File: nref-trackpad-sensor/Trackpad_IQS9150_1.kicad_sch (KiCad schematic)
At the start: 49 parts, among them CN1 FPC_6PIN, IC1 IQS9150-000QFR

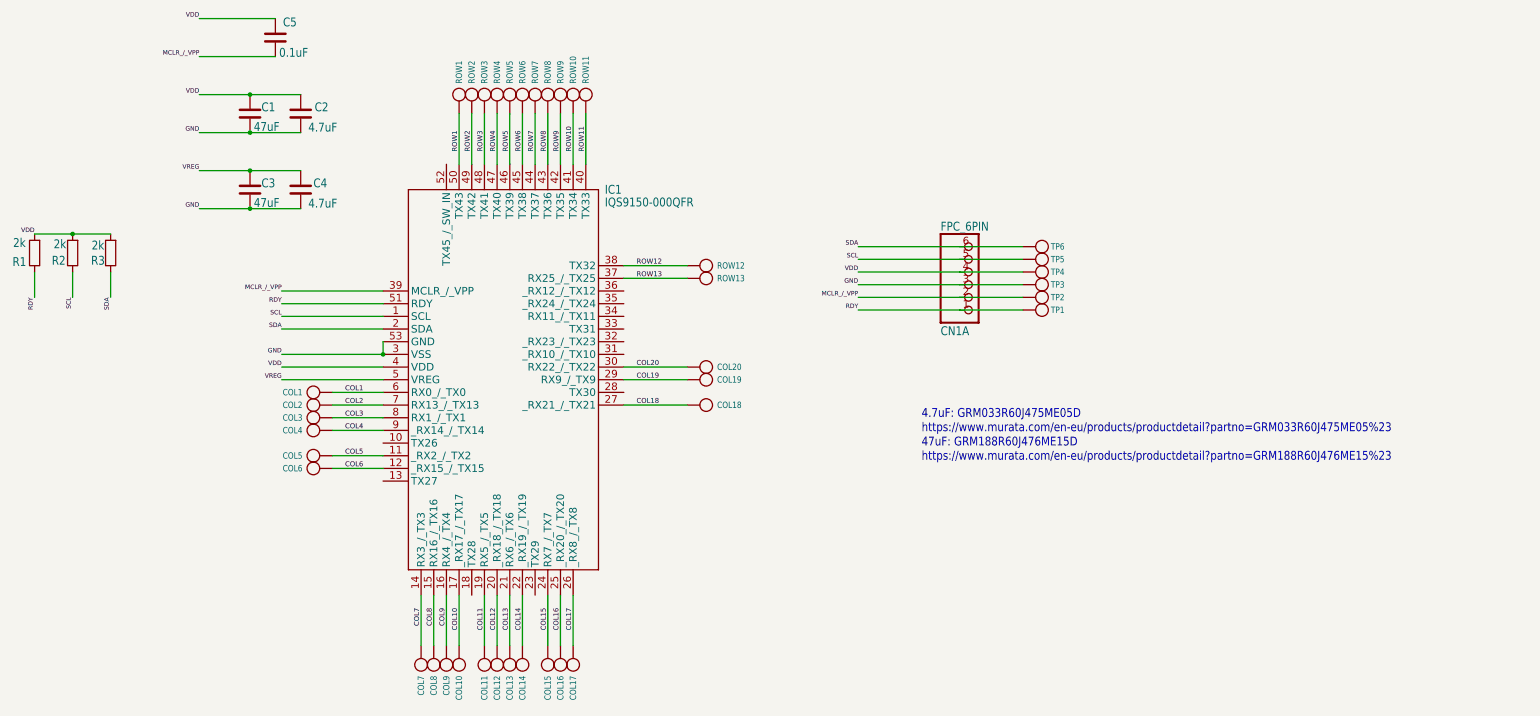
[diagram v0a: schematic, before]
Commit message: trackpad sensor: redesign pcb shape for production
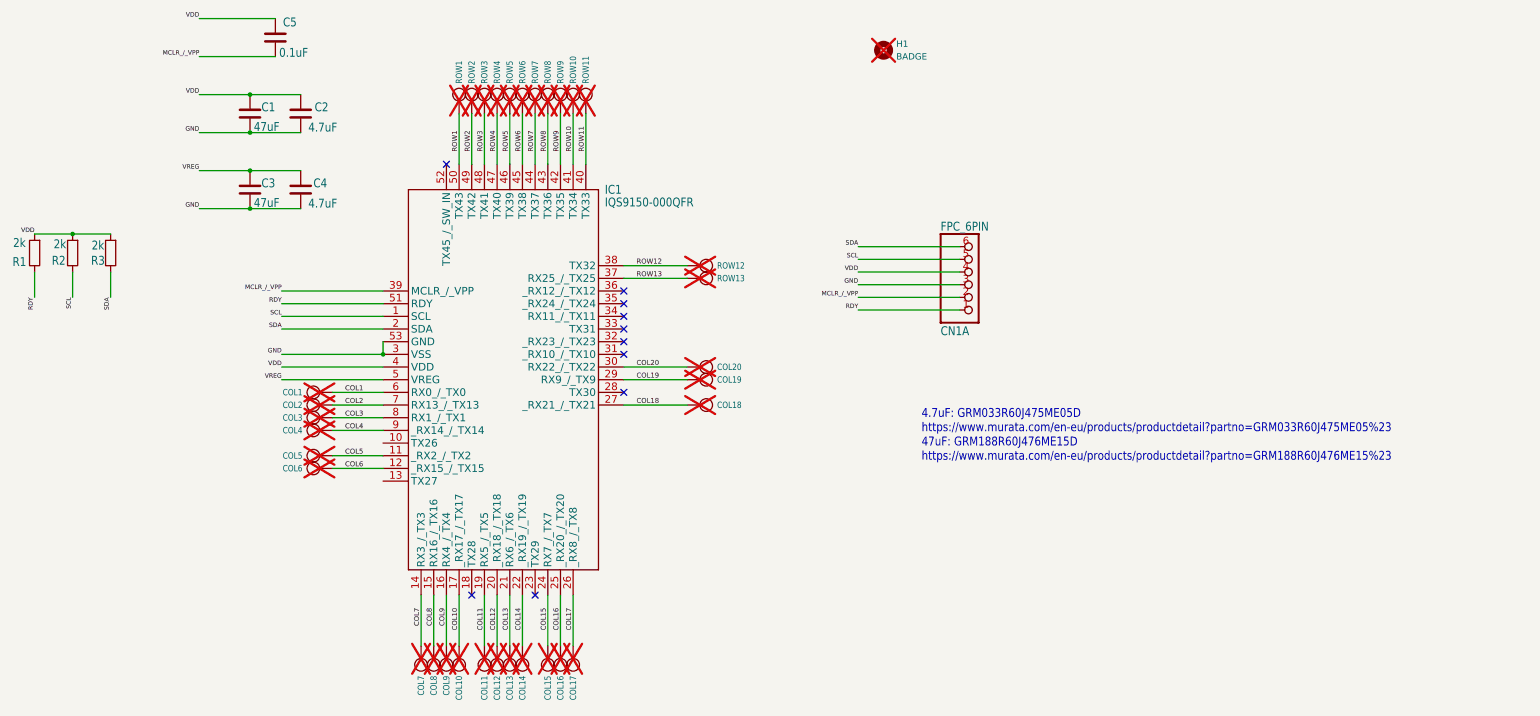
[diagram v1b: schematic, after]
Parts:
- removed TP1, TP2, TP3, TP4, TP5, TP6: TESTPOINTROUND1.5MMNO, Trackpad_IQS9150:TESTPOINT_ROUND_1.5MM_NO, symbol Trackpad_IQS9150:TESTPOINTROUND1.5MMNO
- added H1: BADGE, footprints:nref-tpsensor-badge, symbol Mechanical:MountingHole
- C1, C3: LCSC (none) -> C140782; MPN (none) -> GRM188R60J476ME15D; Manufacturer (none) -> Murata
- C2, C4: footprint Capacitor_SMD:C_0201_0603Metric -> Capacitor_SMD:C_0402_1005Metric; LCSC (none) -> C23733; MPN (none) -> CL05A475MP5NRNC; Manufacturer (none) -> Samsung
- C5: footprint Capacitor_SMD:C_0201_0603Metric -> Capacitor_SMD:C_0402_1005Metric; LCSC (none) -> C1525; MPN (none) -> CL05B104KO5NNNC; Manufacturer (none) -> Samsung
- CN1: LCSC (none) -> C202118; MPN (none) -> FH12-6S-0.5SH(55); Manufacturer (none) -> Hirose
- COL1, COL10, COL11, COL12, COL13, COL14, COL15, COL16, COL17, COL18, COL19, COL2, COL20, COL3, COL4, COL5, COL6, COL7, COL8, COL9, ROW1, ROW10, ROW11, ROW12, ROW13, ROW2, ROW3, ROW4, ROW5, ROW6, ROW7, ROW8, ROW9: now not fitted; now left out of the parts list
- IC1: LCSC (none) -> C34066848; MPN (none) -> IQS9150-000QFR; Manufacturer (none) -> Azoteq
- R1, R2, R3: LCSC (none) -> C4109; MPN (none) -> 0402WGF2001TCE; Manufacturer (none) -> Uni-Royal
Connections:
- no-connect marks 0 -> 10
